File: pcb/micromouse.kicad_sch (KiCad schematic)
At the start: 6 parts, among them U1 TSSP77038ETR, U2 TSSP77038ETR, U3 TSSP77038ETR, U4 TSSP77038ETR, U5 TSSP77038ETR, U6 TSSP77038ETR

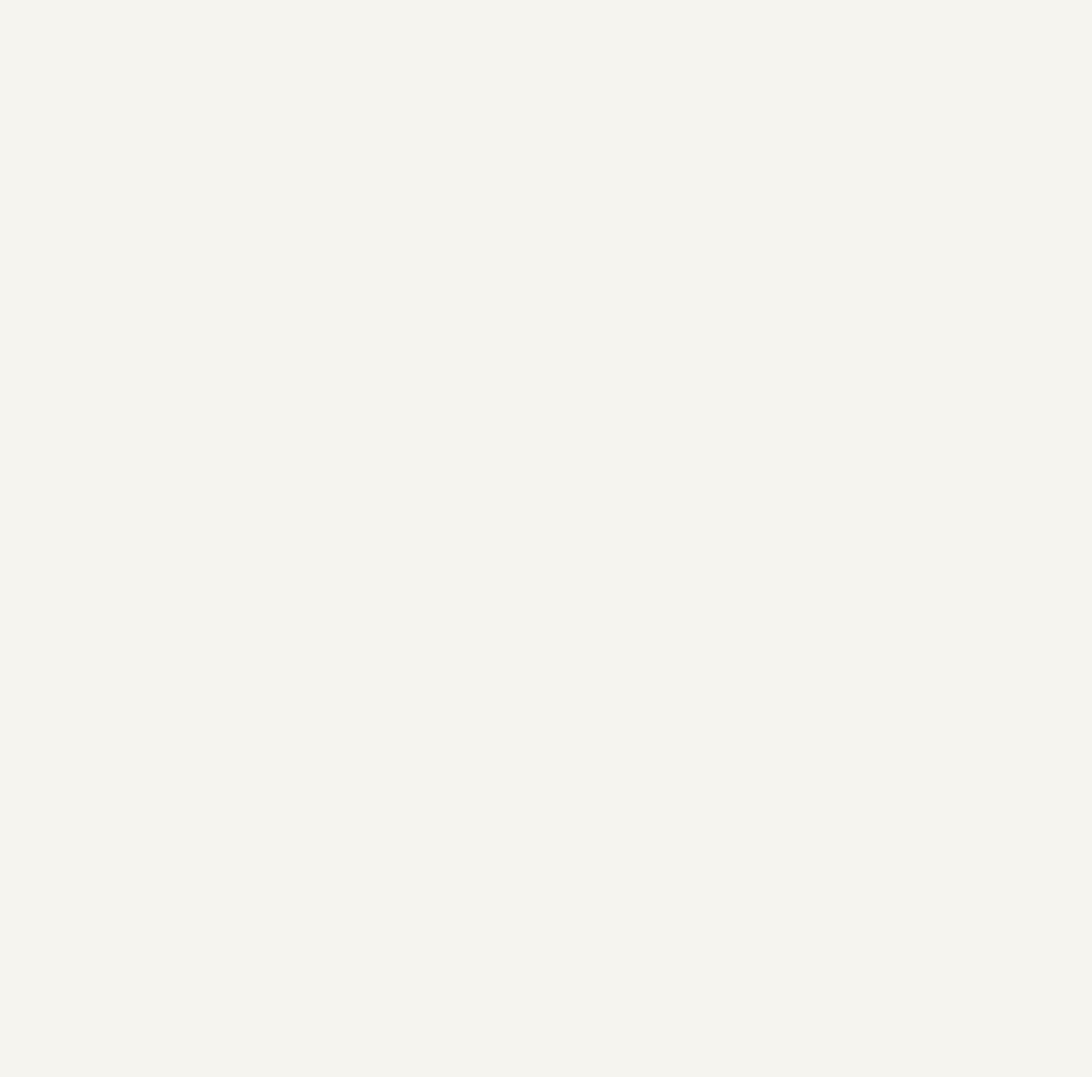
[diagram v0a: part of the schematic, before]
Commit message: add mcu
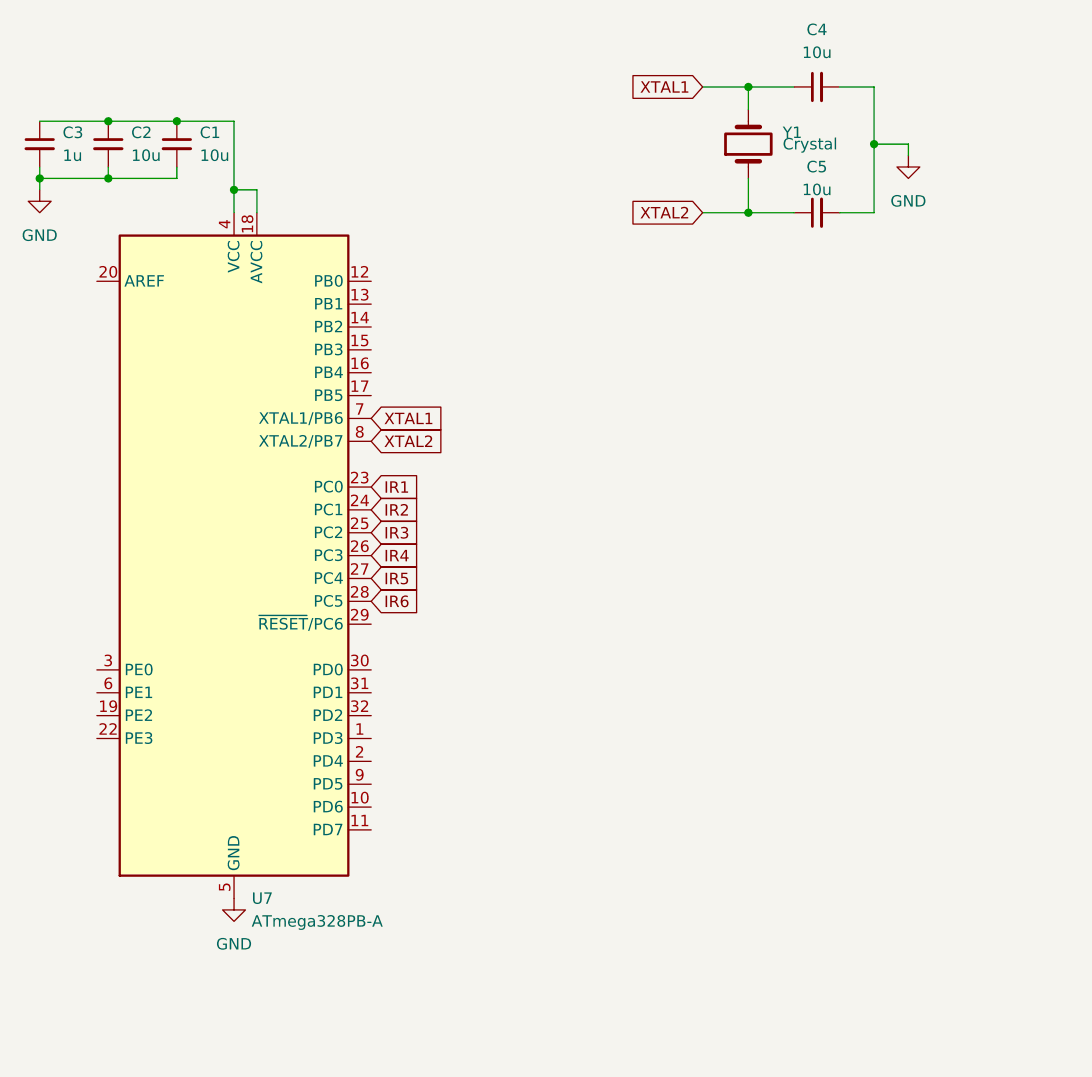
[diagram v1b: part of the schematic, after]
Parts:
- added C1, C2, C4, C5: 10u, symbol Device:C_Small
- added C3: 1u, symbol Device:C_Small
- added U7: ATmega328PB-A, Package_QFP:TQFP-32_7x7mm_P0.8mm, symbol MCU_Microchip_ATmega:ATmega328PB-A
- added Y1: Crystal, symbol Device:Crystal
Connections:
- net GND: now also C1.2, C2.2, C3.2, C4.2, C5.2, U7.21 (GND), U7.5 (GND)
- net IR1: now also U7.23 (PC0)
- net IR2: now also U7.24 (PC1)
- net IR3: now also U7.25 (PC2)
- net IR4: now also U7.26 (PC3)
- net IR5: now also U7.27 (PC4)
- net IR6: now also U7.28 (PC5)
- new net: C1.1, C2.1, C3.1, U7.18 (AVCC), U7.4 (VCC)
- new net XTAL1: C4.1, U7.7 (XTAL1/PB6), Y1.2
- new net XTAL2: C5.1, U7.8 (XTAL2/PB7), Y1.1

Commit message: add program port
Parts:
- added J1: AVR-ISP-6, symbol Connector:AVR-ISP-6
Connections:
- net +3.3V: now also C1.1, C2.1, C3.1, U7.18 (AVCC), U7.4 (VCC), J1.2 (VCC)
- net GND: now also J1.6 (GND)
- new net MISO: J1.1 (MISO)
- new net MOSI: J1.4 (MOSI)
- new net RST: J1.5 (~{RST})
- new net SCK: J1.3 (SCK)
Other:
- moved on the sheet: C1, C2, C3

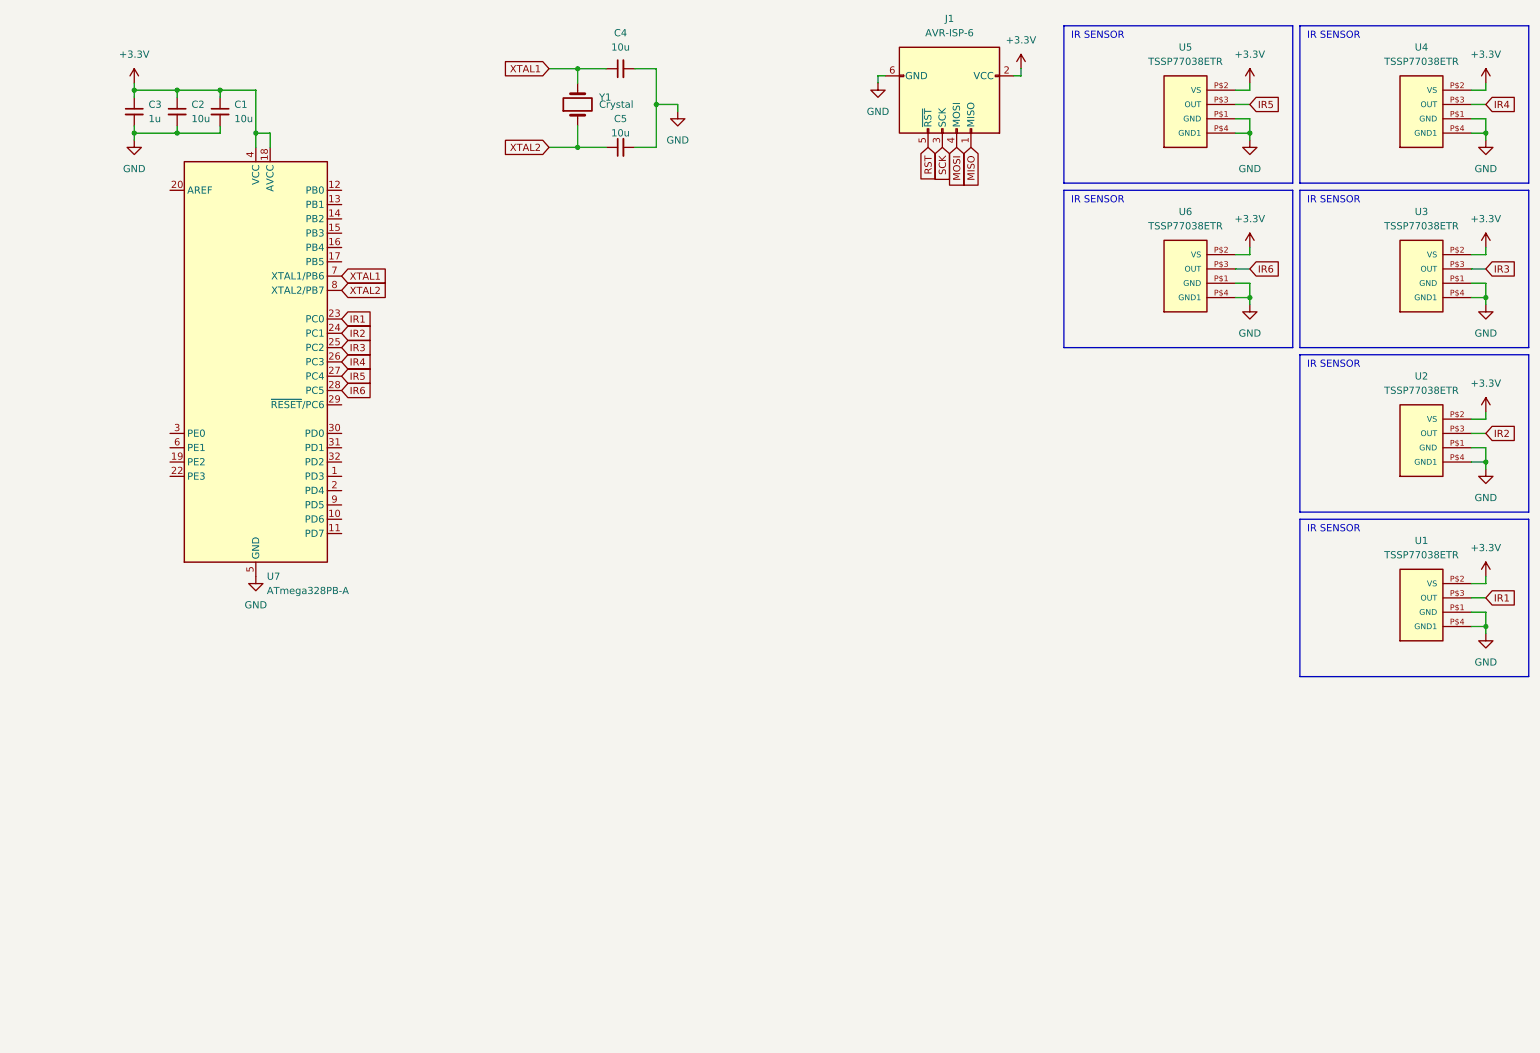
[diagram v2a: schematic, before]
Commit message: wiring mcu program port
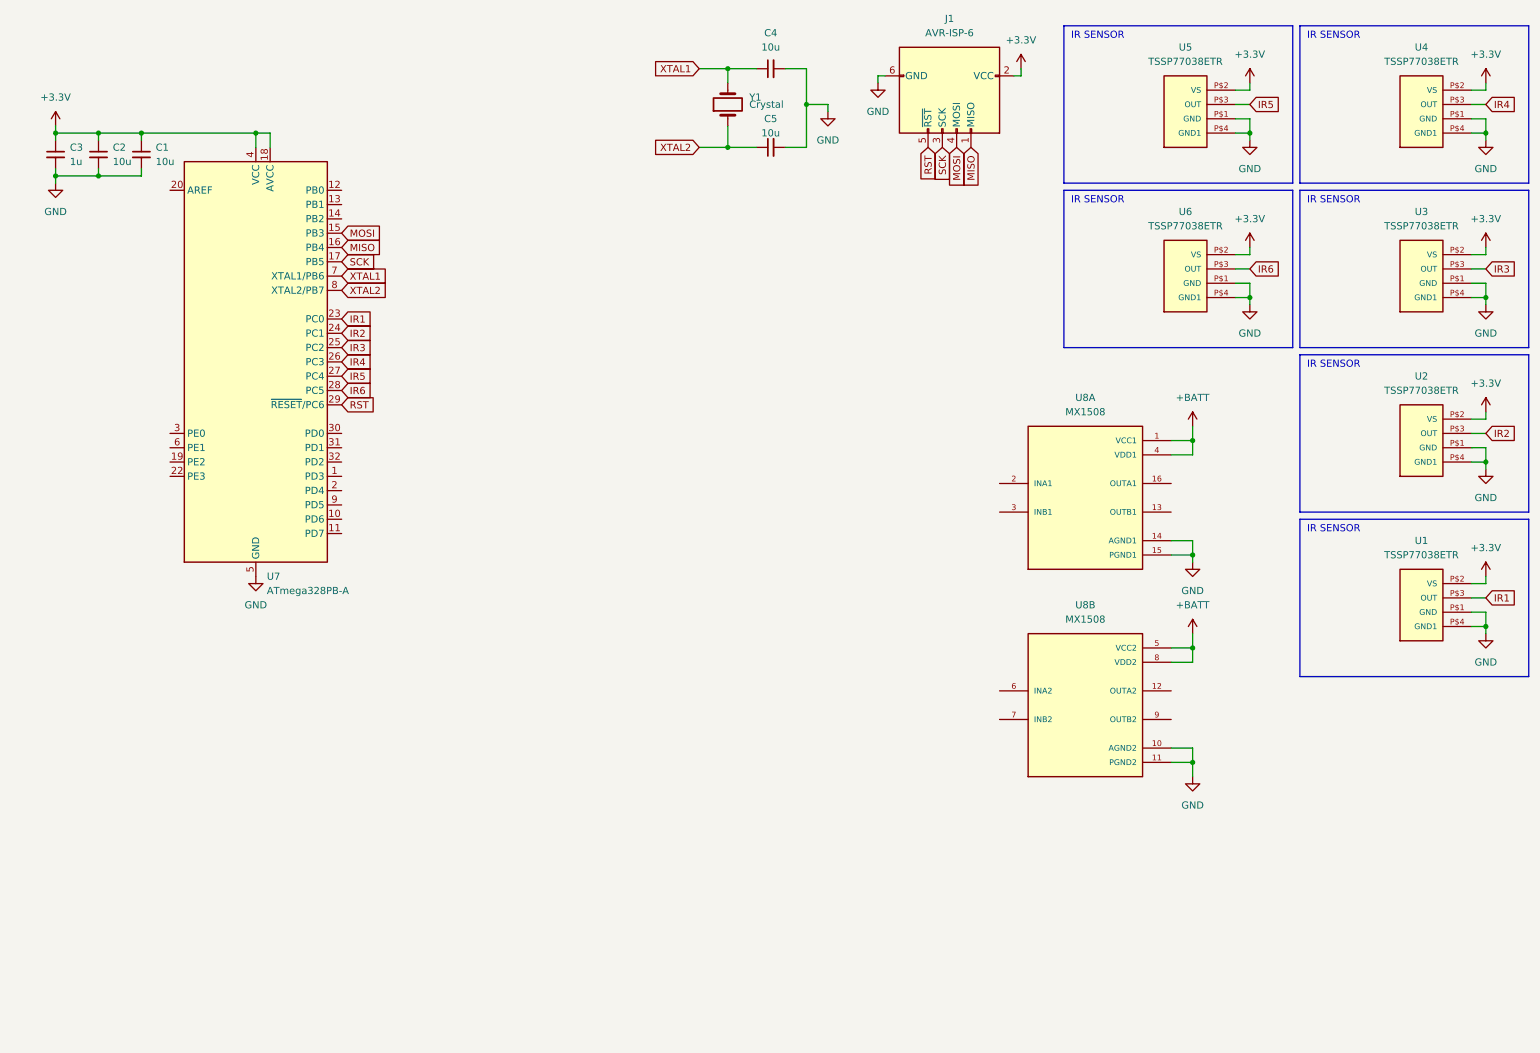
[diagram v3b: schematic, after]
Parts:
- added U8: MX1508, MX1508:SOIC127P600X177-16N, symbol MX1508:MX1508
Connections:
- net GND: now also U8.10 (AGND2), U8.11 (PGND2), U8.14 (AGND1), U8.15 (PGND1)
- net MISO: now also U7.16 (PB4)
- net MOSI: now also U7.15 (PB3)
- net RST: now also U7.29 (~{RESET}/PC6)
- net SCK: now also U7.17 (PB5)
- new net +BATT: U8.1 (VCC1), U8.4 (VDD1), U8.5 (VCC2), U8.8 (VDD2)
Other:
- moved on the sheet: C1, C2, C3, C4, C5, Y1
